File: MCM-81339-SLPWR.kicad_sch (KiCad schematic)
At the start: 17 parts, among them J2 Conn_01x02, U4 VN7040ASTR

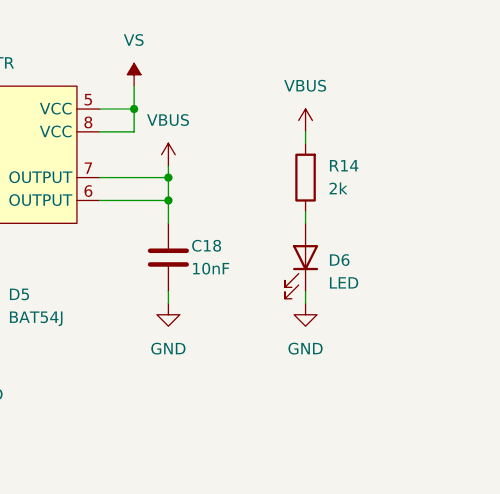
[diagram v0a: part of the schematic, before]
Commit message: add protection on uart, add fab outputs
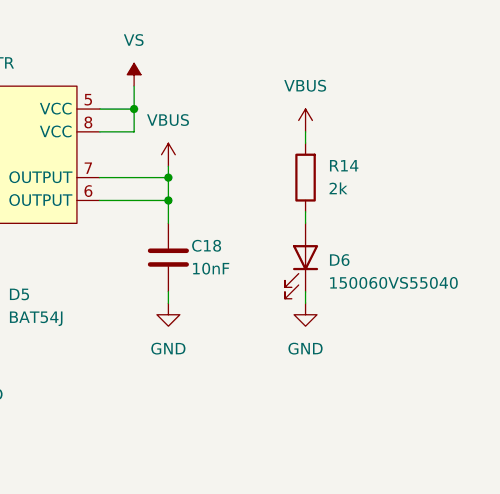
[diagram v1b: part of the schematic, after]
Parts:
- D6: value LED -> 150060VS55040
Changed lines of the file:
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@@
       (effects (font (size 1.27 1.27)) (justify left))
     )
-    (property "Value" "LED" (id 1) (at 190.5 109.5374 90)
+    (property "Value" "150060VS55040" (id 1) (at 190.5 109.5374 90)
       (effects (font (size 1.27 1.27)) (justify left))
     )
